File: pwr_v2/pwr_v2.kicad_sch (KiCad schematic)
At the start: 22 parts, among them M1 Conn_02x03_Counter_Clockwise, M2 Conn_02x03_Counter_Clockwise, M3 Conn_02x03_Counter_Clockwise, M4 Conn_02x03_Counter_Clockwise, Q1 BUK9832-55A, SW1 SW_SPST

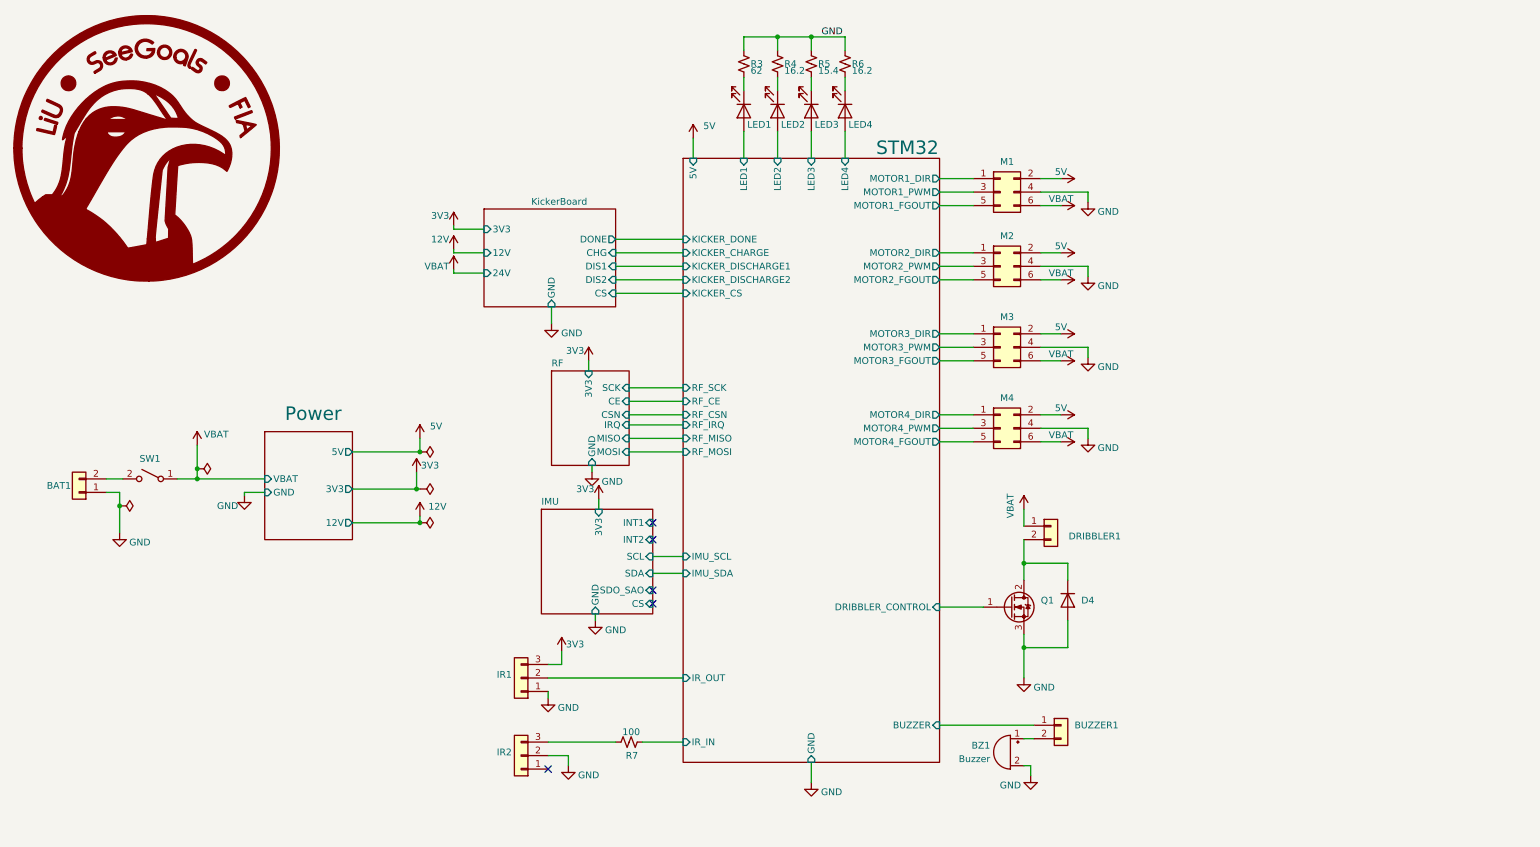
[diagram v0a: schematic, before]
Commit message: File structure enhanced.
Added uniform titleblocks and 3D renders for easier view, file cleanups.
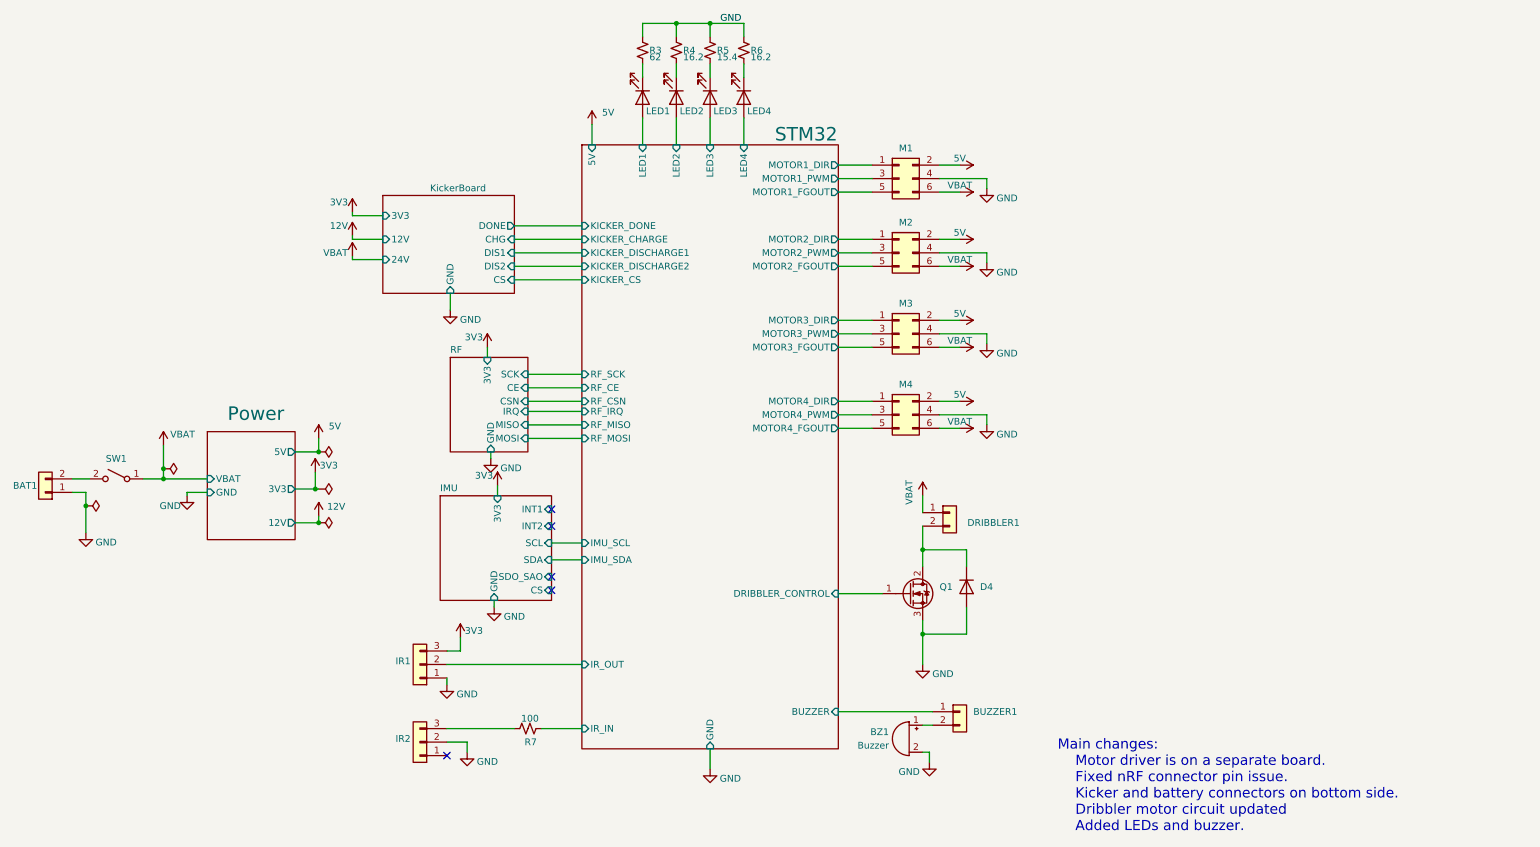
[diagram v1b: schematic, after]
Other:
- note added: "Main changes: Motor driver is on a separate board. Fixed nRF connector pin issue. Kicker and battery connectors on bottom side. Dribbler motor circuit updated Added LEDs and buzzer."
- company: (none) -> Buck regulator circuits to generate 12V, 5V and 3.3V supplies.
- title: pwr_v2 -> Power board
- moved on the sheet: BAT1, BUZZER1, BZ1, D4, DRIBBLER1, IR1, IR2, LED1, LED2, LED3, LED4, M1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
